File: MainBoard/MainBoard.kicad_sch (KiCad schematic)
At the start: 19 parts, among them J1 1761681-3, U1 TL072CP

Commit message: some updates for clarity
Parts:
- V1: now not fitted; now left out of the parts list
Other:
- note added: ".options method=gear .options gmin=1e-9 cshunt=1e-12 .options reltol=1e-2 abstol=1e-9 vntol=1e-6 .options itl1=300 itl4=300 .options maxstep=100p .options temp=60 .ic v(Output)=0 .tran 10u 25u uic .control run plot v(Trigger) v(Output) .endc"
- note removed: ".options method=gear .options gmin=1e-9 cshunt=1e-12 .options reltol=1e-2 abstol=1e-9 vntol=1e-6 .options itl1=300 itl4=300 .options maxstep=100p .ic v(Output)=0 .tran 10u 200u uic .control run set hcopyps set hcopywidth=800 set hcopyheight=600 hardcopy out.ps v(Trigger) v(Output) .endc"
- moved on the sheet: C1, C2, C3, C4, C5, C8, D1, D2, D3, D6, F1, F2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

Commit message: plotting currents
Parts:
- added V2: 12, symbol Simulation_SPICE:VDC
- added V3: -12, symbol Simulation_SPICE:VDC
- C8: value 1.0uF -> 10nf
- R0: value 150K -> 15K
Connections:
- net +v: now also V2.1
- net -v: now also V3.1
- net GND: now also U1.6 (2IN-), U1.7 (2OUT), V2.2, V3.2
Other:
- note added: ".options method=gear .options gmin=1e-9 cshunt=1e-12 .options reltol=1e-2 abstol=1e-9 vntol=1e-6 .options itl1=300 itl4=300 .options maxstep=100p .options temp=60 .tran 10u 10us .control run plot v(Trigger) v(Output) V(Net-_D1-K_) V(Net-_D1-A_) v(Net-_D6-A_) plot i(R0) i(R1) i(R2) i(R3) i(C2) i(C8) i(D1) i(D6) .endc"
- note removed: ".options method=gear .options gmin=1e-9 cshunt=1e-12 .options reltol=1e-2 abstol=1e-9 vntol=1e-6 .options itl1=300 itl4=300 .options maxstep=100p .options temp=60 .ic v(Output)=0 .tran 10u 25u uic .control run plot v(Trigger) v(Output) .endc"
- moved on the sheet: C1, C3, C4, C5, D2, D3, F1, F2, J1

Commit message: functional fix attack and decay
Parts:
- R3: value 30K -> 1k
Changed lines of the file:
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@@
 			)
 		)
-		(property "Value" "30K"
+		(property "Value" "1k"
 			(at 59.944 75.438 90)
 			(effects

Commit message: added some addition TODO notes
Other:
- note added: "TODO: Add Rail Clamps to limit output to supply voltages Add resister on output to for reverse input protection Add rail Clamps to input signal Add reister on input for protection Swap R3 w/ POT to control decay Swap R0 w/ POT to control attack Adopt Trigger input to be Gate input Use Gate falling edge to control when release starts Use comparator w/ POT to control threshold to determine sustain 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"
- company: (none) -> R-mods
- title: (none) -> Envelope Generator
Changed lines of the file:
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@@
 	(generator_version "9.0")
 	(paper "A4")
+	(title_block
+		(title "Envelope Generator")
+		(date "2025-10-05")
+		(rev "0.1b")
+		(company "R-mods")
+	)
+	(text "TODO:\nAdd Rail Clamps to limit output to supply voltages\nAdd resister on output to for reverse input protection\nAdd rail Clamps to input signal\nAdd reister on input for protection\nSwap R3 w/ POT to control decay\nSwap R0 w/ POT to control attack\nAdopt Trigger input to be Gate input\nUse Gate falling edge to control when release starts\nUse comparator w/ POT to control threshold to determine sustain level\nKeep in mind the need for a diode switching circuit\n\n"
+		(exclude_from_sim no)
+		(at 203.2 47.244 0)
+		(effects
+			(font
+				(size 1.27 1.27)
+			)
+			(justify left)
+		)
+	)
 	(text ".options method=gear \n.options gmin=1e-9 cshunt=1e-12 \n.options reltol=1e-2 abstol=1e-9 vntol=1e-6 \n.options itl1=300 itl4=300 \n.options maxstep=100p\n.options temp=60\n.tran 10u 10us\n.control\nrun\nplot v(Trigger) v(Output) V(Net-_D1-K_) V(Net-_D1-A_) v(Net-_D6-A_)\nplot i(R0) i(R1) i(R2) i(R3) i(C2) i(C8) i(D1) i(D6)\n.endc\n"
 		(exclude_from_sim no)

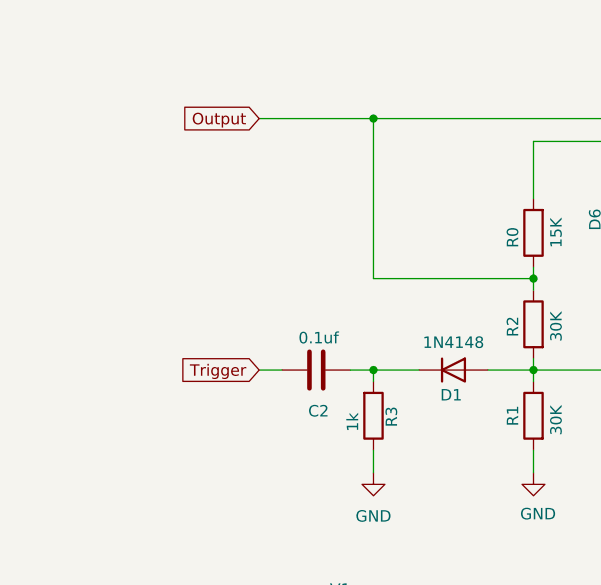
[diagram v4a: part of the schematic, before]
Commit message: added D4 clamp to ground on output to keep evenlope positive
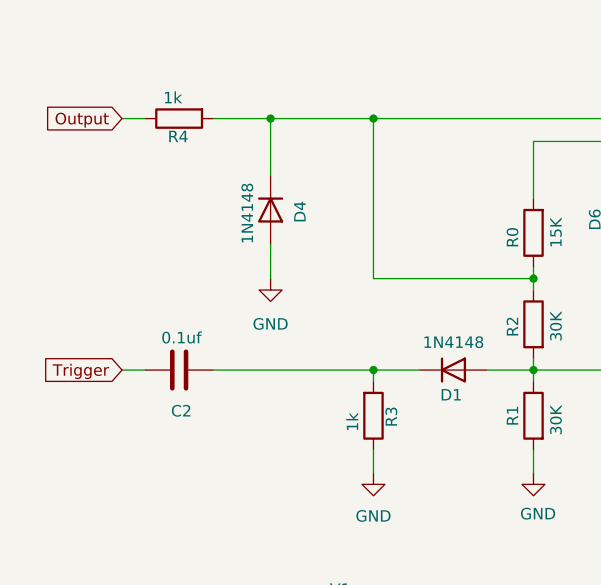
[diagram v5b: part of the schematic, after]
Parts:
- added D4: 1N4148, symbol Device:D
- added R4: 1k, symbol Device:R
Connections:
- net GND: now also D4.2 (A)
- net Output: now also R4.1; no longer R0.1, R2.1, U1.1 (1OUT)
- new net: D4.1 (K), R0.1, R2.1, R4.2, U1.1 (1OUT)
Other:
- moved on the sheet: C2

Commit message: updated notes
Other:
- note added: "TODO: Add Rail Clamps to limit output to supply voltages Add rail Clamps to limit input signal to supply voltages Add resister to input signal for protection Swap R3 w/ POT to control decay Swap R0 w/ POT to control attack Adopt Trigger input to be Gate input Use Gate falling edge to control when release starts Use comparator w/ POT to control threshold to determine sustain level Keep in mind the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"
- note removed: "TODO: Add Rail Clamps to limit output to supply voltages Add resister on output to for reverse input protection Add rail Clamps to input signal Add reister on input for protection Swap R3 w/ POT to control decay Swap R0 w/ POT to control attack Adopt Trigger input to be Gate input Use Gate falling edge to control when release starts Use comparator w/ POT to control threshold to determine sustain 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"
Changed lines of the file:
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@@
 		(company "R-mods")
 	)
-	(text "TODO:\nAdd Rail Clamps to limit output to supply voltages\nAdd resister on output to for reverse input protection\nAdd rail Clamps to input signal\nAdd reister on input for protection\nSwap R3 w/ POT to control decay\nSwap R0 w/ POT to control attack\nAdopt Trigger input to be Gate input\nUse Gate falling edge to control when release starts\nUse comparator w/ POT to control threshold to determine sustain level\nKeep in mind the need for a diode switching circuit\n\n"
+	(text "TODO:\nAdd Rail Clamps to limit output to supply voltages\nAdd rail Clamps to limit input signal to supply voltages\nAdd resister to input signal for protection\nSwap R3 w/ POT to control decay\nSwap R0 w/ POT to control attack\nAdopt Trigger input to be Gate input\nUse Gate falling edge to control when release starts\nUse comparator w/ POT to control threshold to determine sustain level\nKeep in mind the need for a diode switching circuit\n\n"
 		(exclude_from_sim no)
 		(at 203.2 47.244 0)

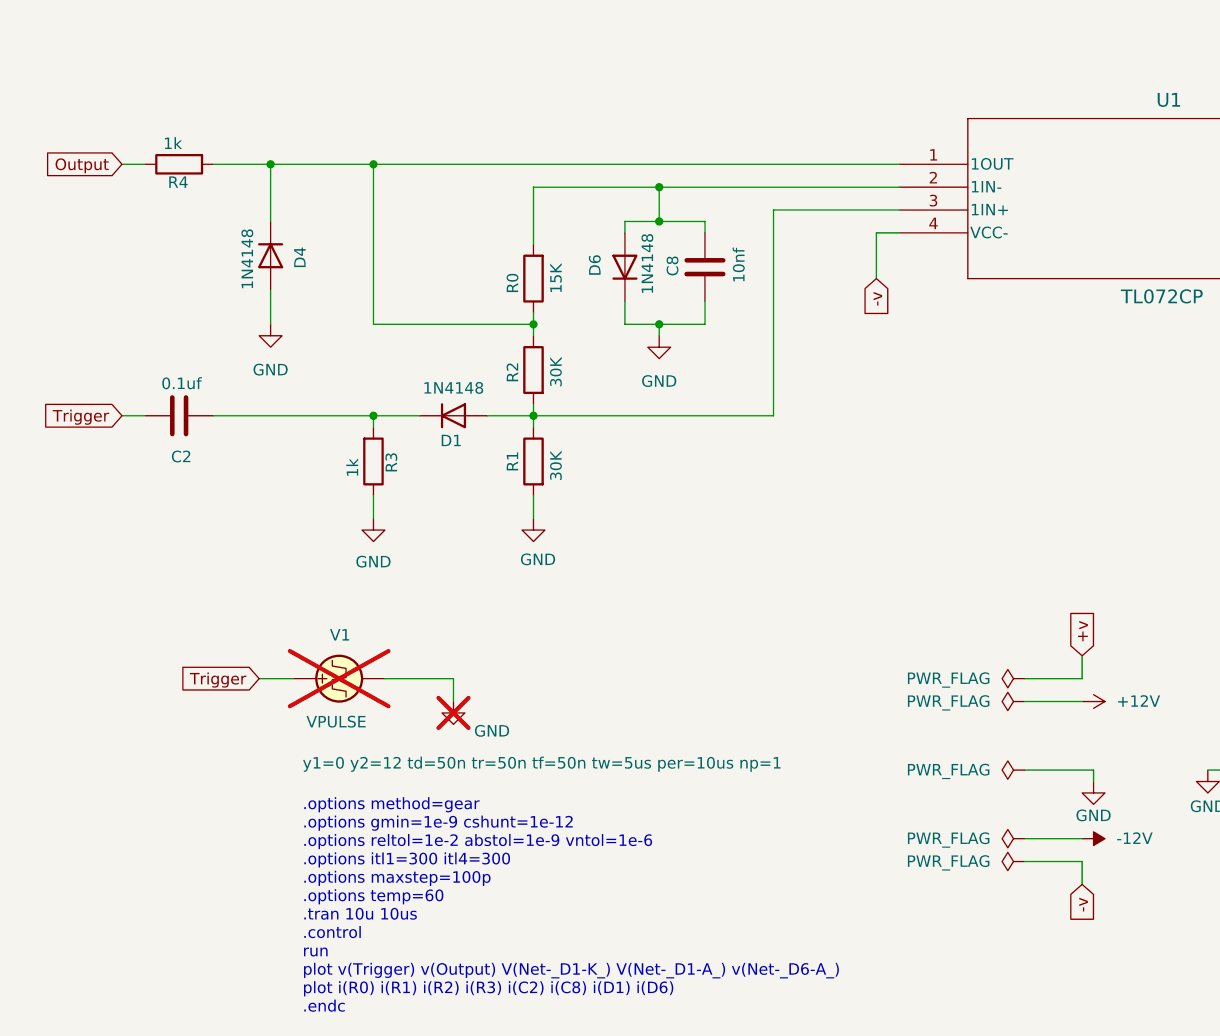
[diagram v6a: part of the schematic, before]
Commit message: renamed trigger to gate, modified simulation to use +5V gate signal instead of +12V
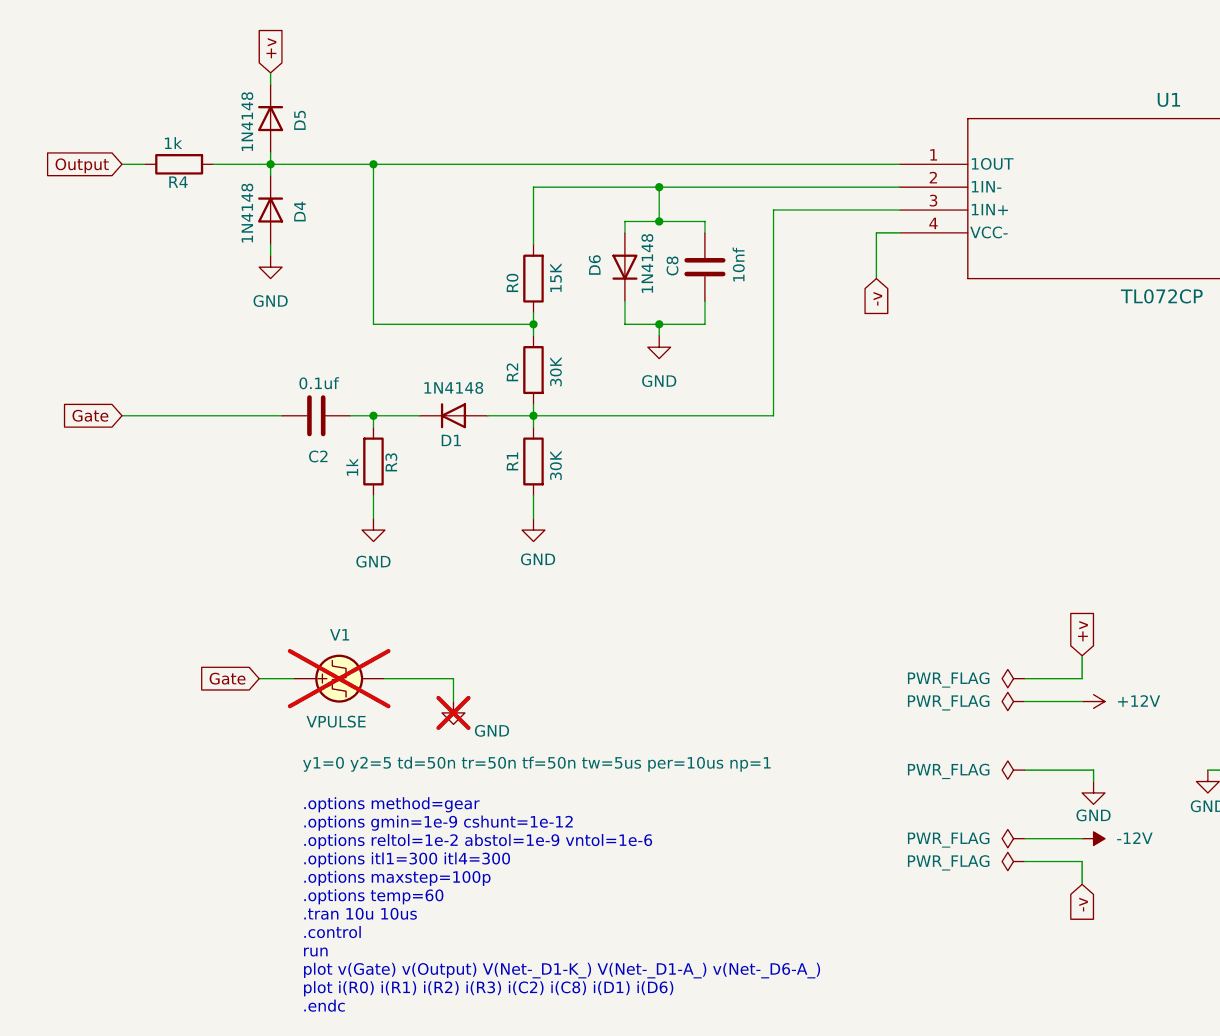
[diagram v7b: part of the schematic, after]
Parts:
- added D5: 1N4148, symbol Device:D
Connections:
- net +v: now also D5.1 (K)
- net at D4.1 (K), R0.1, R2.1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: now also D5.2 (A)
- net Trigger renamed Gate
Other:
- note added: ".options method=gear .options gmin=1e-9 cshunt=1e-12 .options reltol=1e-2 abstol=1e-9 vntol=1e-6 .options itl1=300 itl4=300 .options maxstep=100p .options temp=60 .tran 10u 10us .control run plot v(Gate) v(Output) V(Net-_D1-K_) V(Net-_D1-A_) v(Net-_D6-A_) plot i(R0) i(R1) i(R2) i(R3) i(C2) i(C8) i(D1) i(D6) .endc"
- note removed: ".options method=gear .options gmin=1e-9 cshunt=1e-12 .options reltol=1e-2 abstol=1e-9 vntol=1e-6 .options itl1=300 itl4=300 .options maxstep=100p .options temp=60 .tran 10u 10us .control run plot v(Trigger) v(Output) V(Net-_D1-K_) V(Net-_D1-A_) v(Net-_D6-A_) plot i(R0) i(R1) i(R2) i(R3) i(C2) i(C8) i(D1) i(D6) .endc"
- moved on the sheet: C2, D4
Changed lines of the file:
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@@
 		)
 	)
-	(text ".options method=gear \n.options gmin=1e-9 cshunt=1e-12 \n.options reltol=1e-2 abstol=1e-9 vntol=1e-6 \n.options itl1=300 itl4=300 \n.options maxstep=100p\n.options temp=60\n.tran 10u 10us\n.control\nrun\nplot v(Trigger) v(Output) V(Net-_D1-K_) V(Net-_D1-A_) v(Net-_D6-A_)\nplot i(R0) i(R1) i(R2) i(R3) i(C2) i(C8) i(D1) i(D6)\n.endc\n"
+	(text ".options method=gear \n.options gmin=1e-9 cshunt=1e-12 \n.options reltol=1e-2 abstol=1e-9 vntol=1e-6 \n.options itl1=300 itl4=300 \n.options maxstep=100p\n.options temp=60\n.tran 10u 10us\n.control\nrun\nplot v(Gate) v(Output) V(Net-_D1-K_) V(Net-_D1-A_) v(Net-_D6-A_)\nplot i(R0) i(R1) i(R2) i(R3) i(C2) i(C8) i(D1) i(D6)\n.endc\n"
 		(exclude_from_sim no)
 		(at 54.356 123.19 0)
@@
 	)
 	(junction
+		(at 62.23 68.58)
+		(diameter 0)
+		(color 0 0 0 0)
+	)
+	(junction
 		(at 237.49 118.11)
 		(diameter 0)
@@
 	)
 	(junction
+		(at 50.8 40.64)
+		(diameter 0)
+		(color 0 0 0 0)
+	)
+	(junction
 		(at 189.23 97.79)
 		(diameter 0)
@@
 	)
 	(junction
-		(at 50.8 40.64)
-		(diameter 0)
-		(color 0 0 0 0)
-	)
-	(junction
-		(at 62.23 68.58)
-		(diameter 0)
-		(color 0 0 0 0)
-	)
-	(junction
 		(at 237.49 97.79)
 		(diameter 0)
@@
 	(wire
 		(pts
+			(xy 59.69 68.58) (xy 62.23 68.58)
+		)
+		(stroke
+			(width 0)
+			(type default)
+		)
+	)
+	(wire
+		(pts
+			(xy 50.8 49.53) (xy 50.8 50.8)
+		)
+		(stroke
+			(width 0)
+			(type default)
+		)
+	)
+	(wire
+		(pts
+			(xy 50.8 40.64) (xy 50.8 41.91)
+		)
+		(stroke
+			(width 0)
+			(type default)
+		)
+	)
+	(wire
+		(pts
 			(xy 161.29 95.25) (xy 161.29 96.52)
 		)
@@
 	(wire
 		(pts
-			(xy 36.83 68.58) (xy 34.29 68.58)
+			(xy 34.29 68.58) (xy 52.07 68.58)
 		)
 		(stroke
@@
 	(wire
 		(pts
-			(xy 50.8 40.64) (xy 62.23 40.64)
+			(xy 44.45 40.64) (xy 50.8 40.64)
 		)
 		(stroke
@@
 	(wire
 		(pts
-			(xy 44.45 68.58) (xy 62.23 68.58)
+			(xy 50.8 39.37) (xy 50.8 40.64)
 		)
 		(stroke
@@
 	(wire
 		(pts
-			(xy 50.8 40.64) (xy 44.45 40.64)
+			(xy 80.01 58.42) (xy 80.01 57.15)
 		)
 		(stroke
@@
 	(wire
 		(pts
-			(xy 80.01 58.42) (xy 80.01 57.15)
+			(xy 189.23 106.68) (xy 189.23 107.95)
 		)
 		(stroke
@@
 	(wire
 		(pts
-			(xy 189.23 106.68) (xy 189.23 107.95)
+			(xy 201.93 97.79) (xy 201.93 99.06)
 		)
 		(stroke
@@
 	(wire
 		(pts
-			(xy 201.93 97.79) (xy 201.93 99.06)
+			(xy 50.8 30.48) (xy 50.8 31.75)
 		)
 		(stroke
@@
 	(wire
 		(pts
-			(xy 50.8 46.99) (xy 50.8 40.64)
+			(xy 142.24 109.22) (xy 142.24 107.95)
 		)
 		(stroke
@@
 	(wire
 		(pts
-			(xy 142.24 109.22) (xy 142.24 107.95)
+			(xy 237.49 106.68) (xy 241.3 106.68)
 		)
 		(stroke
@@
 	(wire
 		(pts
-			(xy 237.49 106.68) (xy 241.3 106.68)
+			(xy 74.93 68.58) (xy 80.01 68.58)
 		)
 		(stroke
@@
 	(wire
 		(pts
-			(xy 74.93 68.58) (xy 80.01 68.58)
+			(xy 50.8 40.64) (xy 62.23 40.64)
 		)
 		(stroke
@@
 	(wire
 		(pts
-			(xy 50.8 54.61) (xy 50.8 58.42)
-		)
-		(stroke
-			(width 0)
-			(type default)
-		)
-	)
-	(wire
-		(pts
 			(xy 237.49 96.52) (xy 237.49 97.79)
 		)
@@
 		)
 	)
-	(global_label "Trigger"
+	(global_label "Gate"
 		(shape input)
 		(at 34.29 68.58 180)
@@
 		)
 		(property "Intersheetrefs" "${INTERSHEET_REFS}"
-			(at 24.7734 68.58 0)
+			(at 27.0715 68.58 0)
 			(effects
 				(font
@@
 	(global_label "+v"
 		(shape input)
+		(at 50.8 30.48 90)
+		(fields_autoplaced yes)
+		(effects
+			(font
+				(size 1.27 1.27)
+			)
+			(justify left)
+		)
+		(property "Intersheetrefs" "${INTERSHEET_REFS}"
+			(at 50.8 24.9548 90)
+			(effects
+				(font
+					(size 1.27 1.27)
+				)
+				(justify left)
+				(hide yes)
+			)
+		)
+	)
+	(global_label "+v"
+		(shape input)
 		(at 140.97 95.25 90)
 		(fields_autoplaced yes)
@@
 		)
 	)
-	(global_label "Trigger"
+	(global_label "Gate"
 		(shape input)
 		(at 49.53 97.79 180)
@@
 		)
 		(property "Intersheetrefs" "${INTERSHEET_REFS}"
-			(at 40.0134 97.79 0)
+			(at 42.3115 97.79 0)
 			(effects
 				(font
@@
 			)
 		)
-		(property "Sim.Params" "y1=0 y2=12 td=50n tr=50n tf=50n tw=5us per=10us np=1"
+		(property "Sim.Params" "y1=0 y2=5 td=50n tr=50n tf=50n tw=5us per=10us np=1"
 			(at 54.356 107.188 90)
 			(effects
@@
 	)
 	(symbol
+		(lib_id "Device:D")
+		(at 50.8 35.56 270)
+		(unit 1)
+		(exclude_from_sim no)
+		(in_bom yes)
+		(on_board yes)
+		(dnp no)
+		(property "Reference" "D5"
+			(at 54.102 34.544 0)
+			(effects
+				(font
+					(size 1.27 1.27)
+				)
+				(justify left)
+			)
+		)
+		(property "Value" "1N4148"
+			(at 48.26 32.512 0)
+			(effects
+				(font
+					(size 1.27 1.27)
+				)
+				(justify left)
+			)
+		)
+		(property "Footprint" ""
+			(at 50.8 35.56 0)
+			(effects
+				(font
+					(size 1.27 1.27)
+				)
+				(hide yes)
+			)
+		)
+		(property "Datasheet" "~"
+			(at 50.8 35.56 0)
+			(effects
+				(font
+					(size 1.27 1.27)
+				)
+				(hide yes)
+			)
+		)
+		(property "Description" "Diode"
+			(at 50.8 35.56 0)
+			(effects
+				(font
+					(size 1.27 1.27)
+				)
+				(hide yes)
+			)
+		)
+		(property "Sim.Device" "D"
+			(at 50.8 35.56 0)
+			(effects
+				(font
+					(size 1.27 1.27)
+				)
+				(hide yes)
+			)
+		)
+		(property "Sim.Pins" "1=K 2=A"
+			(at 50.8 35.56 0)
+			(effects
+				(font
+					(size 1.27 1.27)
+				)
+				(hide yes)
+			)
+		)
+		(pin "1"
+		)
+		(pin "2"
+		)
+		(instances
+			(project "MainBoard"
+				(path "/3ec111d7-dc64-45ad-8dee-b084fbabc82e"
+					(reference "D5")
+					(unit 1)
+				)
+			)
+		)
+	)
+	(symbol
 		(lib_id "Device:R")
 		(at 40.64 40.64 90)
@@
 	(symbol
 		(lib_id "Device:C")
-		(at 40.64 68.58 270)
+		(at 55.88 68.58 270)
 		(unit 1)
 		(exclude_from_sim no)
@@
 		(dnp no)
 		(property "Reference" "C2"
-			(at 40.894 73.152 90)
+			(at 56.134 73.152 90)
 			(effects
 				(font
@@
 		)
 		(property "Value" "0.1uf"
-			(at 40.894 65.024 90)
+			(at 56.134 65.024 90)
 			(effects
 				(font
@@
 		)
 		(property "Footprint" ""
-			(at 36.83 69.5452 0)
+			(at 52.07 69.5452 0)
 			(effects
 				(font
@@
 		)
 		(property "Datasheet" "~"
-			(at 40.64 68.58 0)
+			(at 55.88 68.58 0)
 			(effects
 				(font
@@
 		)
 		(property "Description" "Unpolarized capacitor"
-			(at 40.64 68.58 0)
+			(at 55.88 68.58 0)
 			(effects
 				(font
@@
 	(symbol
 		(lib_id "Device:D")
-		(at 50.8 50.8 270)
+		(at 50.8 45.72 270)
 		(unit 1)
 		(exclude_from_sim no)
@@
 		(dnp no)
 		(property "Reference" "D4"
-			(at 54.102 49.784 0)
+			(at 54.102 44.704 0)
 			(effects
 				(font
@@
 		)
 		(property "Value" "1N4148"
-			(at 48.26 47.752 0)
+			(at 48.26 42.672 0)
 			(effects
 				(font
@@
 		)
 		(property "Footprint" ""
-			(at 50.8 50.8 0)
+			(at 50.8 45.72 0)
 			(effects
 				(font
@@
 		)
 		(property "Datasheet" "~"
-			(at 50.8 50.8 0)
+			(at 50.8 45.72 0)
 			(effects
 				(font
@@
 		)
 		(property "Description" "Diode"
-			(at 50.8 50.8 0)
+			(at 50.8 45.72 0)
 			(effects
 				(font
@@
 		)
 		(property "Sim.Device" "D"
-			(at 50.8 50.8 0)
+			(at 50.8 45.72 0)
 			(effects
 				(font
@@
 		)
 		(property "Sim.Pins" "1=K 2=A"
-			(at 50.8 50.8 0)
+			(at 50.8 45.72 0)
 			(effects
 				(font
@@
 	(symbol
 		(lib_id "power:GND")
-		(at 50.8 58.42 0)
+		(at 50.8 50.8 0)
 		(mirror y)
 		(unit 1)
@@
 		(dnp no)
 		(property "Reference" "#PWR012"
-			(at 50.8 64.77 0)
+			(at 50.8 57.15 0)
 			(effects
 				(font
@@
 		)
 		(property "Value" "GND"
-			(at 50.8 63.5 0)
+			(at 50.8 55.88 0)
 			(effects
 				(font
@@
 		)
 		(property "Footprint" ""
-			(at 50.8 58.42 0)
+			(at 50.8 50.8 0)
 			(effects
 				(font
@@
 		)
 		(property "Datasheet" ""
-			(at 50.8 58.42 0)
+			(at 50.8 50.8 0)
 			(effects
 				(font
@@
 		)
 		(property "Description" "Power symbol creates a global label with name \"GND\" , ground"
-			(at 50.8 58.42 0)
+			(at 50.8 50.8 0)
 			(effects
 				(font
